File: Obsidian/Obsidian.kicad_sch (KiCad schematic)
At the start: 4 parts

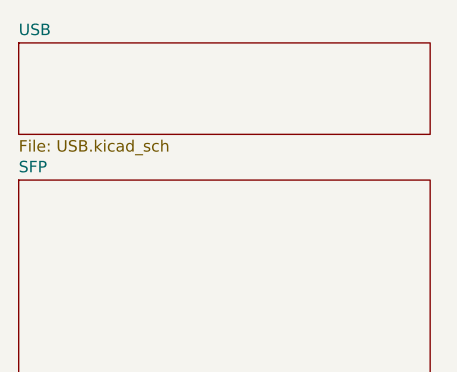
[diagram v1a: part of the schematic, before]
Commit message: adding wago
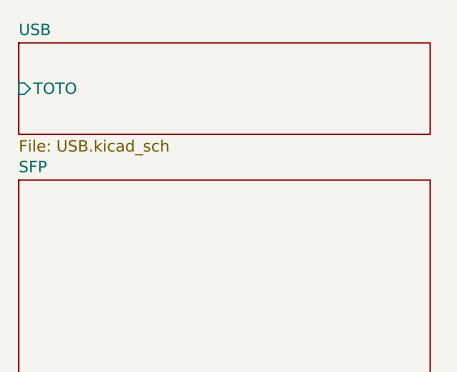
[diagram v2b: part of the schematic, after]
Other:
- sheet USB ports: added TOTO; removed none
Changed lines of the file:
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@@
+			)
+		)
+		(pin "TOTO" input
+			(at 66.04 80.01 180)
+			(effects
+				(font
+					(size 1.27 1.27)
+				)
+				(justify left)
 			)
 		)

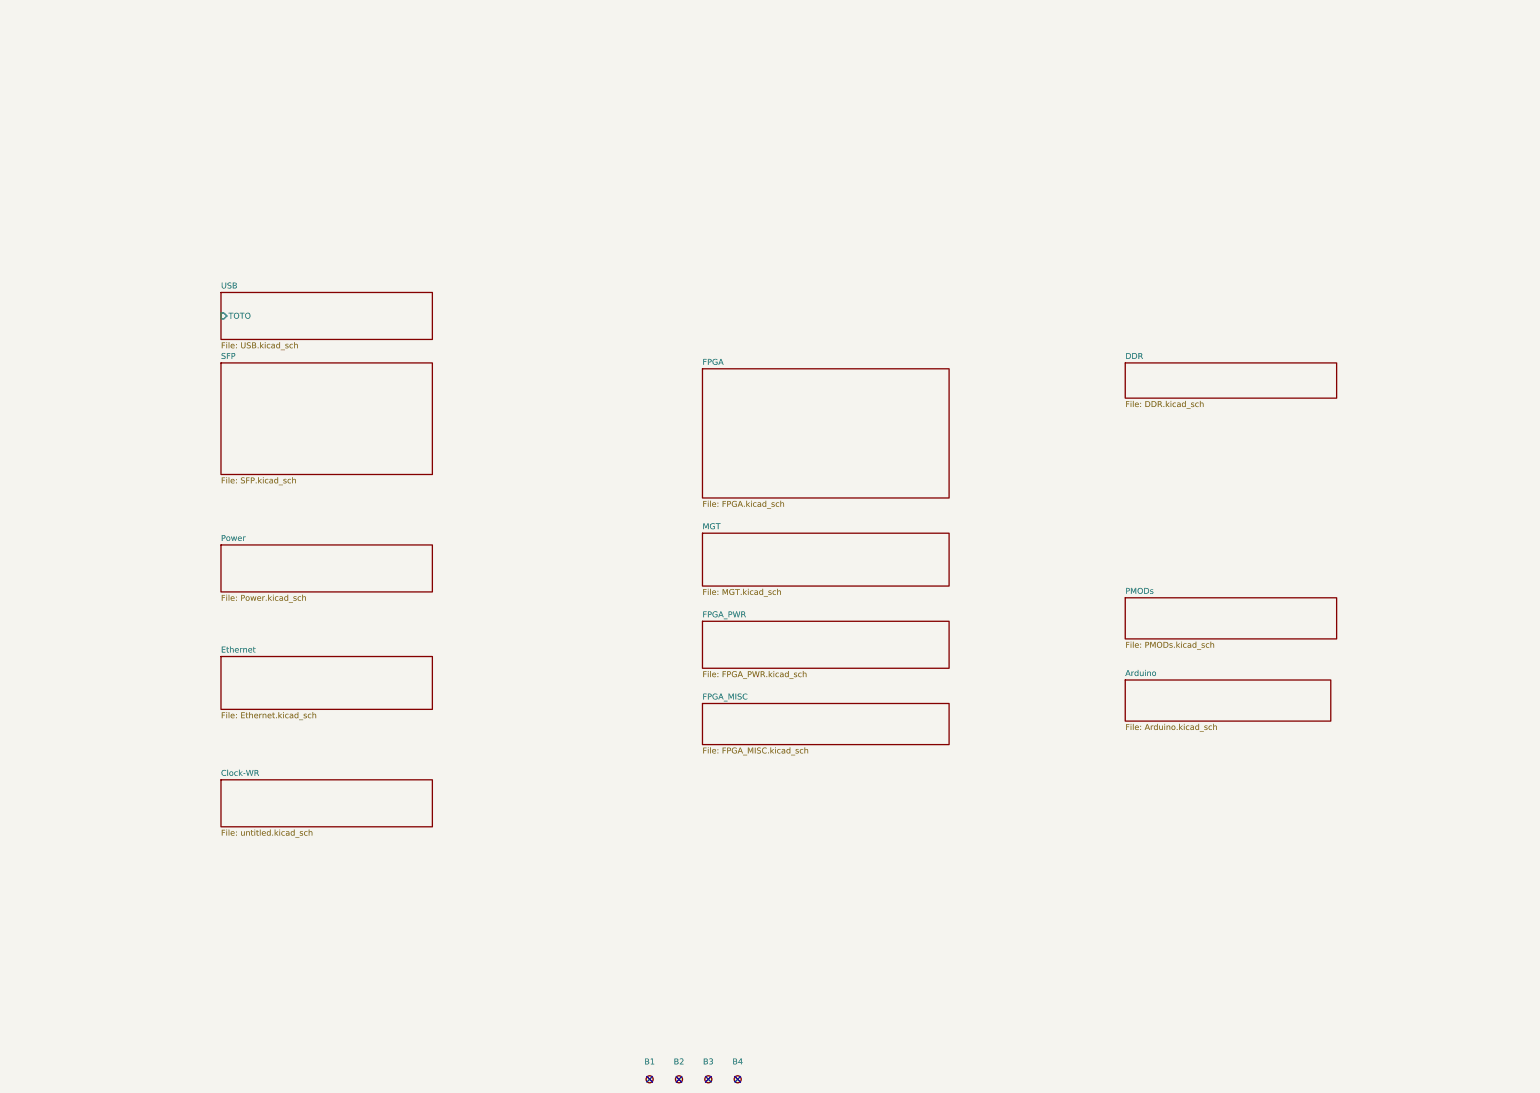
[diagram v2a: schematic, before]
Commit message: replacing global label with hierarchical label
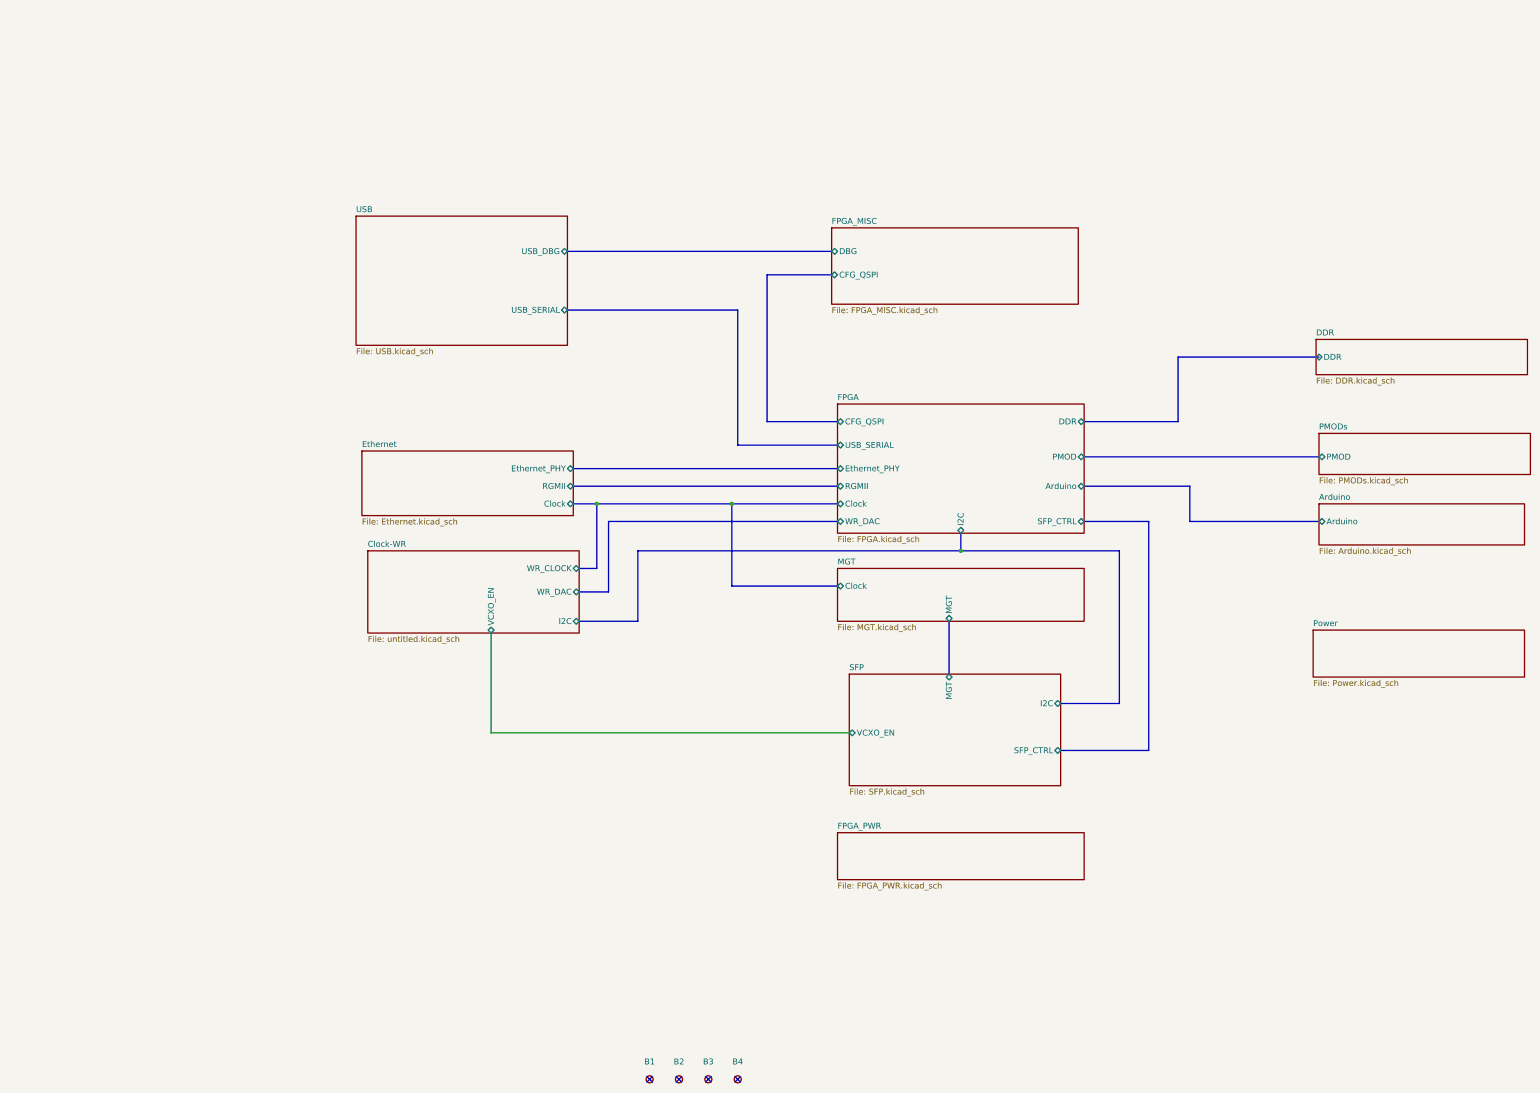
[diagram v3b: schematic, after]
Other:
- sheet Arduino ports: added Arduino; removed none
- sheet Clock-WR ports: added I2C, VCXO_EN, WR_CLOCK, WR_DAC; removed none
- sheet DDR ports: added DDR; removed none
- sheet Ethernet ports: added Clock, Ethernet_PHY, RGMII; removed none
- sheet FPGA ports: added Arduino, CFG_QSPI, Clock, DDR, Ethernet_PHY, I2C, PMOD, RGMII, SFP_CTRL, USB_SERIAL, WR_DAC; removed none
- sheet FPGA_MISC ports: added CFG_QSPI, DBG; removed none
- sheet MGT ports: added Clock, MGT; removed none
- sheet PMODs ports: added PMOD; removed none
- sheet SFP ports: added I2C, MGT, SFP_CTRL, VCXO_EN; removed none
- sheet USB ports: added USB_DBG, USB_SERIAL; removed TOTO

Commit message: Adding symbol library
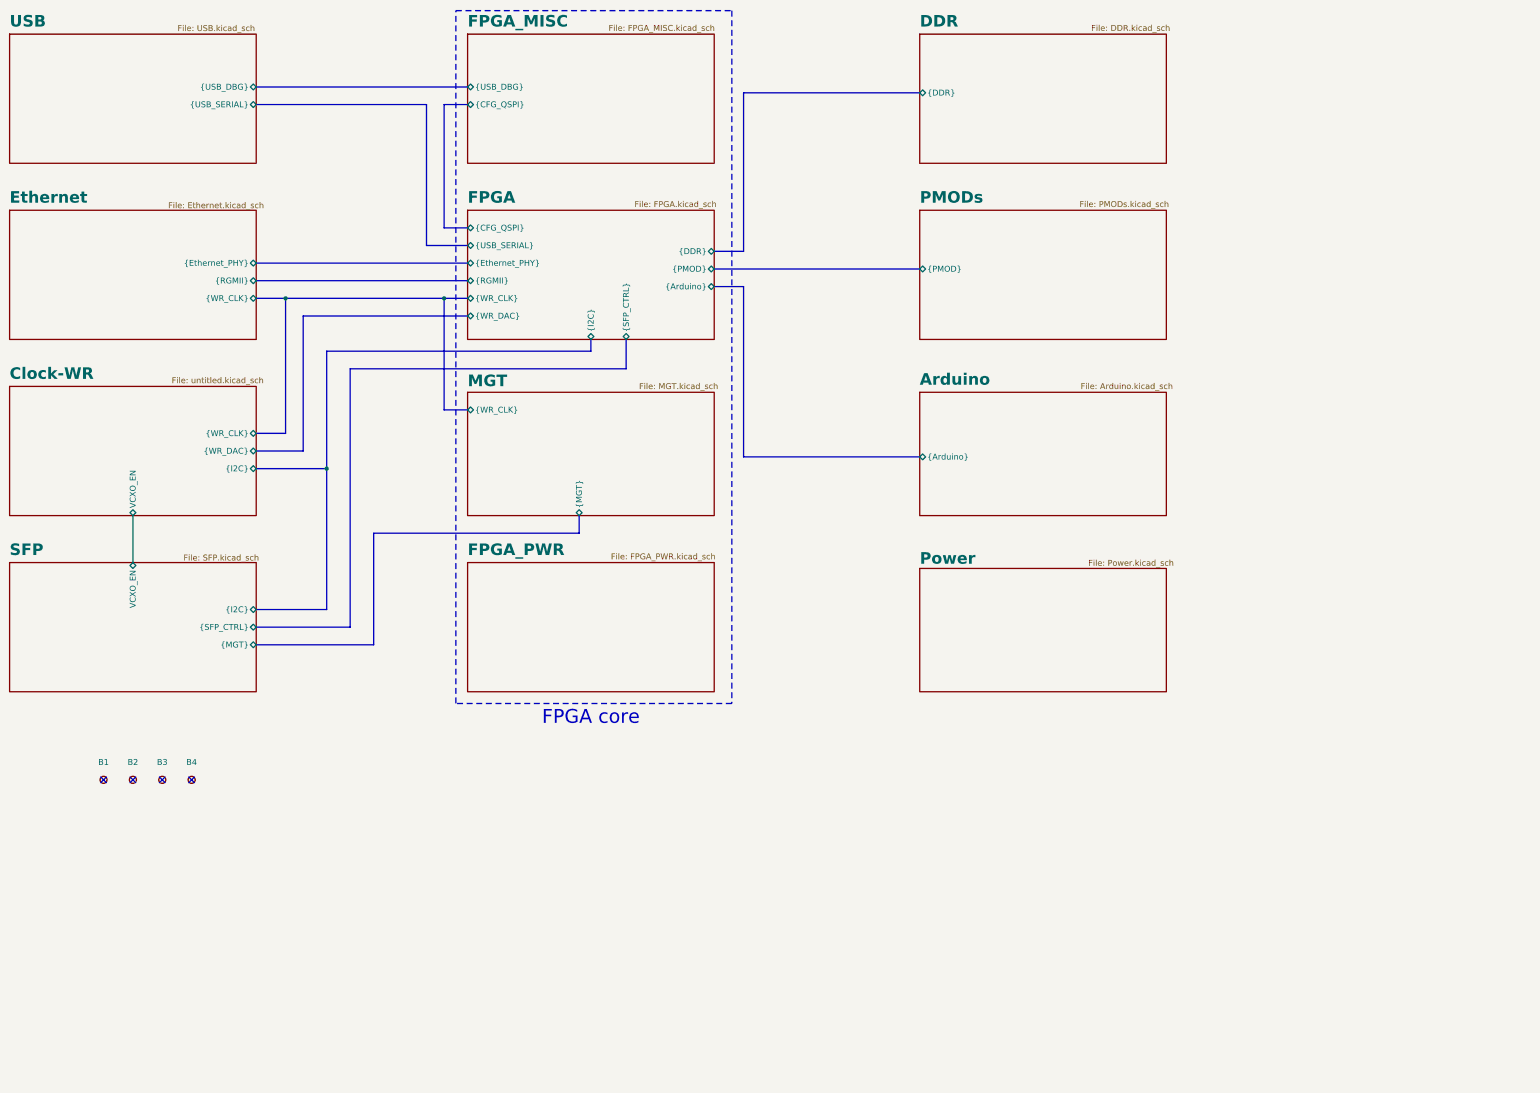
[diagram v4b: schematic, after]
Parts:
- B1, B2, B3, B4: symbol Pads:PLATED_HOLE3.2_PAD5.5 -> Library_Symbol:PLATED_HOLE3.2_PAD5.5
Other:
- sheet Arduino ports: added {Arduino}; removed Arduino
- sheet Clock-WR ports: added {I2C}, {WR_CLK}, {WR_DAC}; removed I2C, WR_CLOCK, WR_DAC
- sheet DDR ports: added {DDR}; removed DDR
- sheet Ethernet ports: added {Ethernet_PHY}, {RGMII}, {WR_CLK}; removed Clock, Ethernet_PHY, RGMII
- sheet FPGA ports: added {Arduino}, {CFG_QSPI}, {DDR}, {Ethernet_PHY}, {I2C}, {PMOD}, {RGMII}, {SFP_CTRL}, {USB_SERIAL}, {WR_CLK}, {WR_DAC}; removed Arduino, CFG_QSPI, Clock, DDR, Ethernet_PHY, I2C, PMOD, RGMII, SFP_CTRL, USB_SERIAL, WR_DAC
- sheet FPGA_MISC ports: added {CFG_QSPI}, {USB_DBG}; removed CFG_QSPI, DBG
- sheet MGT ports: added {MGT}, {WR_CLK}; removed Clock, MGT
- sheet PMODs ports: added {PMOD}; removed PMOD
- sheet SFP ports: added {I2C}, {MGT}, {SFP_CTRL}; removed I2C, MGT, SFP_CTRL
- sheet USB ports: added {USB_DBG}, {USB_SERIAL}; removed USB_DBG, USB_SERIAL
- note added: "FPGA core"
- moved on the sheet: B1, B2, B3, B4

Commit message: Correct Schematic errors
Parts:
- B1, B2, B3, B4: footprint Pads:MTG320_550 -> Footprint:MTG320_550

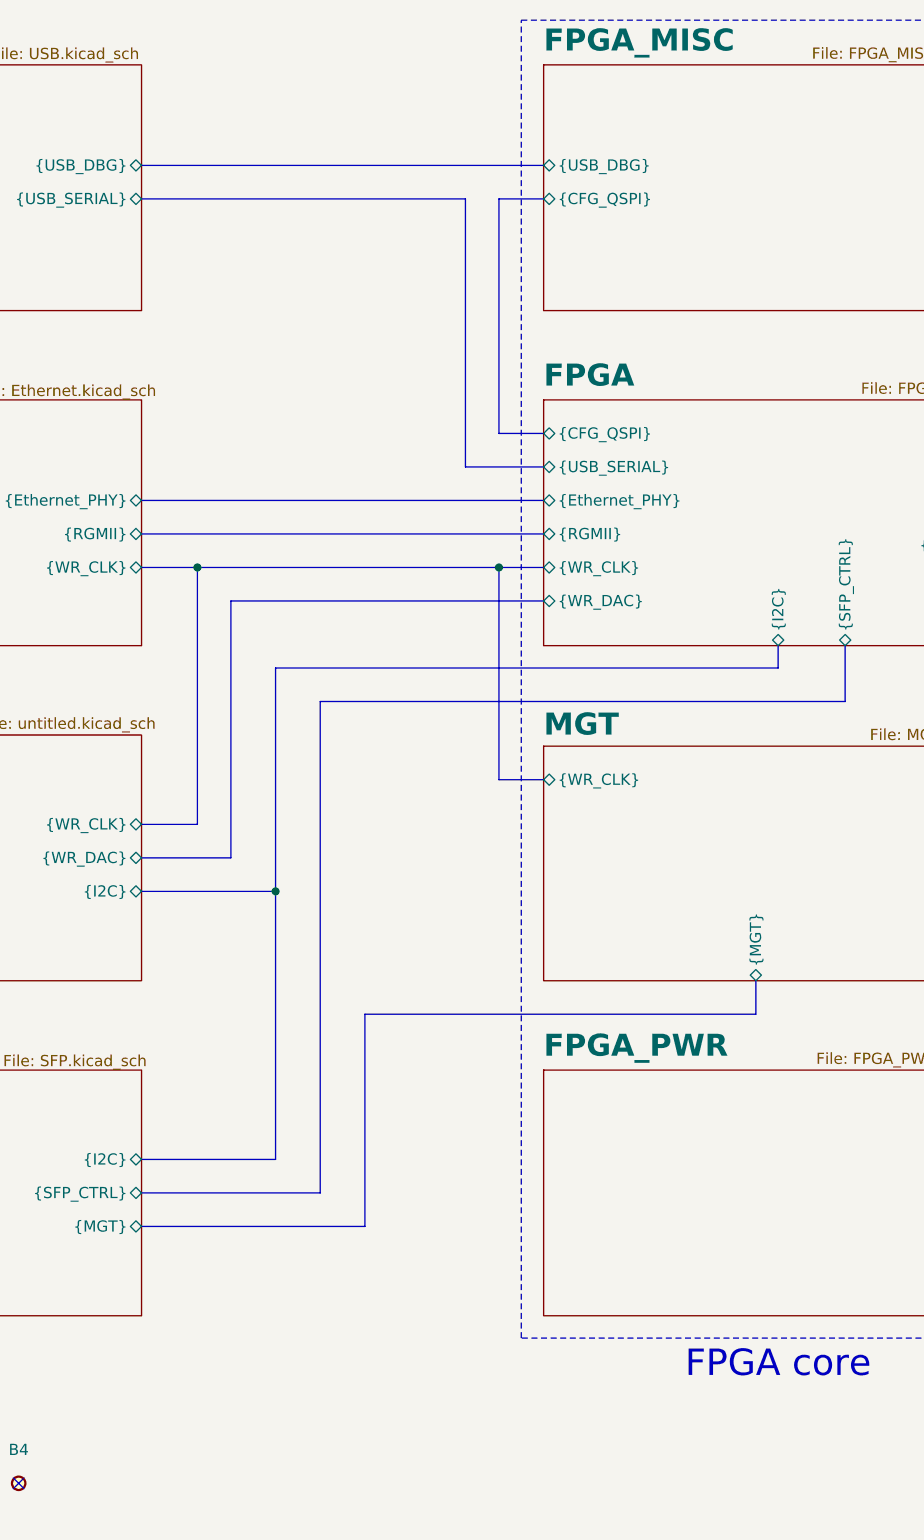
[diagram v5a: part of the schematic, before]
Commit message: adding 3D files, 3D model of twist, and correct DRC
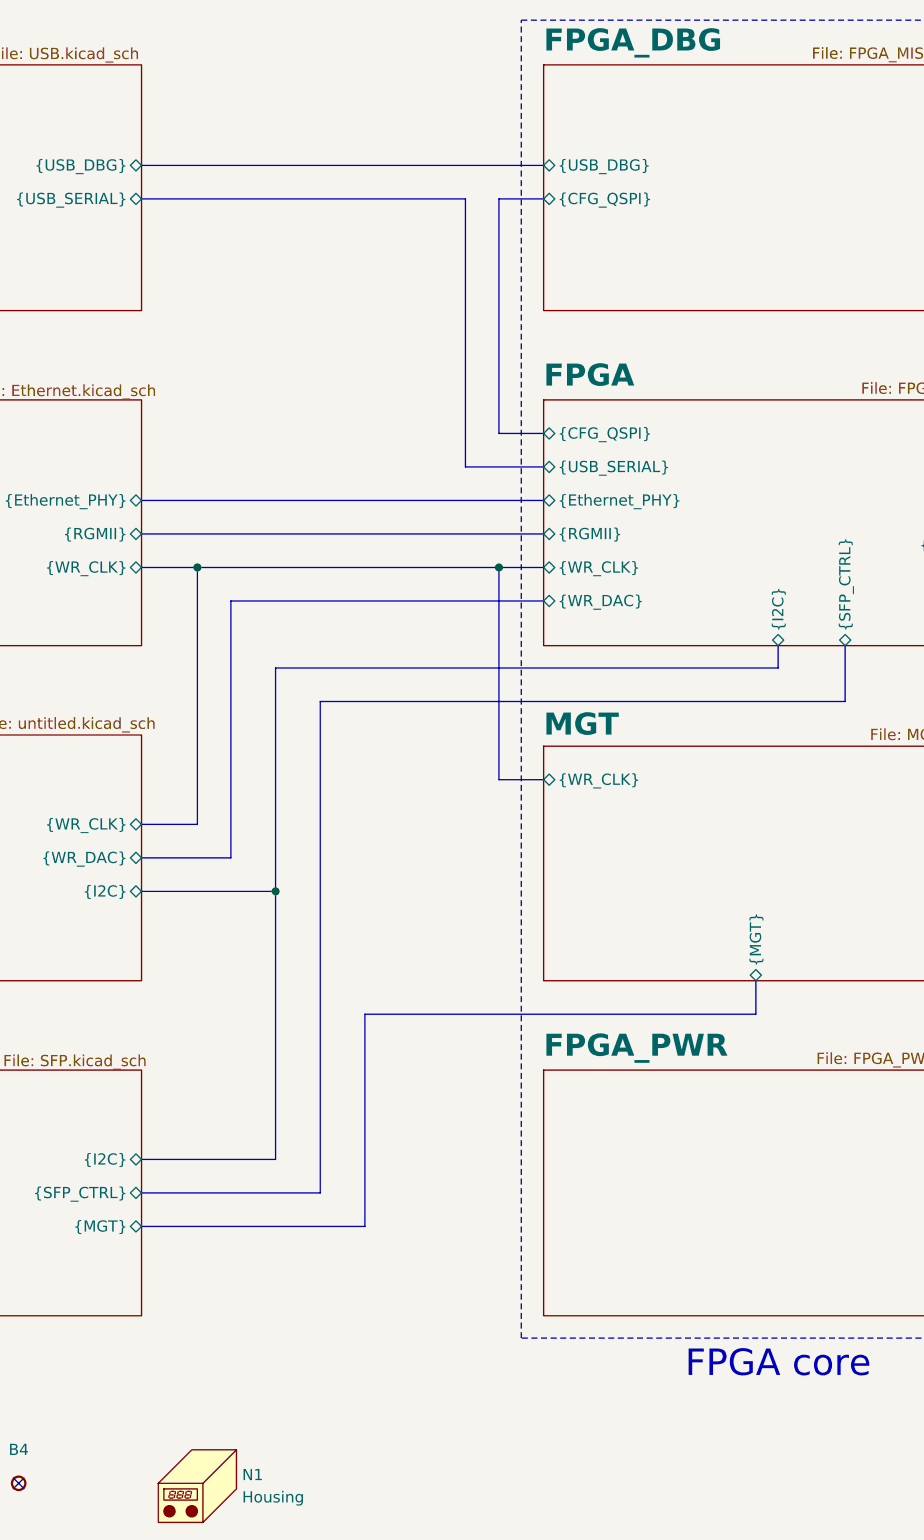
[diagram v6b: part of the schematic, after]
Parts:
- added N1: Housing, Footprint:TWIST, symbol Mechanical:Housing
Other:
- sheet FPGA_MISC renamed FPGA_DBG
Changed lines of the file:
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@@
+	)
+	(symbol
+		(lib_id "Mechanical:Housing")
+		(at 81.28 180.34 0)
+		(unit 1)
+		(exclude_from_sim no)
+		(in_bom yes)
+		(on_board yes)
+		(dnp no)
+		(fields_autoplaced yes)
+		(property "Reference" "N1"
+			(at 85.09 179.3874 0)
+			(effects
+				(font
+					(size 1.27 1.27)
+				)
+				(justify left)
+			)
+		)
+		(property "Value" "Housing"
+			(at 85.09 181.9274 0)
+			(effects
+				(font
+					(size 1.27 1.27)
+				)
+				(justify left)
+			)
+		)
+		(property "Footprint" "Footprint:TWIST"
+			(at 82.55 179.07 0)
+			(effects
+				(font
+					(size 1.27 1.27)
+				)
+				(hide yes)
+			)
+		)
+		(property "Datasheet" "~"
+			(at 82.55 179.07 0)
+			(effects
+				(font
+					(size 1.27 1.27)
+				)
+				(hide yes)
+			)
+		)
+		(property "Description" "Housing"
+			(at 81.28 180.34 0)
+			(effects
+				(font
+					(size 1.27 1.27)
+				)
+				(hide yes)
+			)
+		)
+		(instances
+			(project ""
+				(path "/c2a4f786-b14c-434a-acf7-b20fb2221b0b"
+					(reference "N1")
+					(unit 1)
+				)
+			)
+		)
 	)
 	(symbol
@@
 			(color 128 255 128 1.0000)
 		)
-		(property "Sheetname" "FPGA_MISC"
+		(property "Sheetname" "FPGA_DBG"
 			(at 119.38 17.7234 0)
 			(effects
